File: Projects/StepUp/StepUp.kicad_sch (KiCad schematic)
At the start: 0 parts

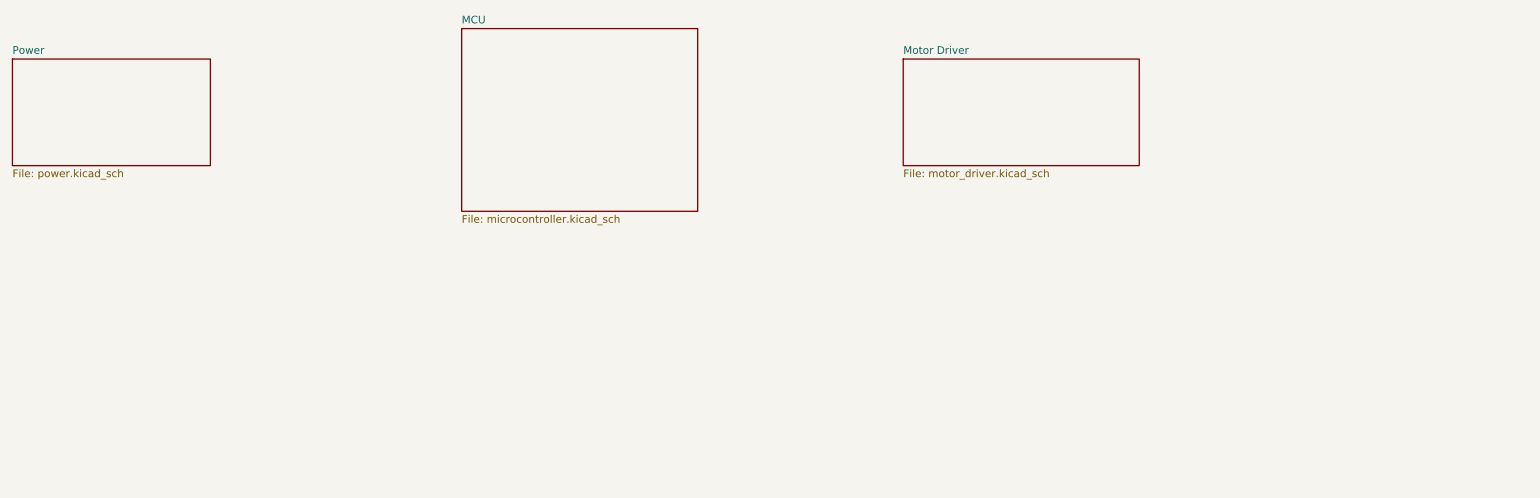
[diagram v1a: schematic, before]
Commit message: feat(rp2040): Layout begins, extra libraries
RPico minimal project downloaded + assets copied. Boost converter layout
in progress, 18650 battery holder added.
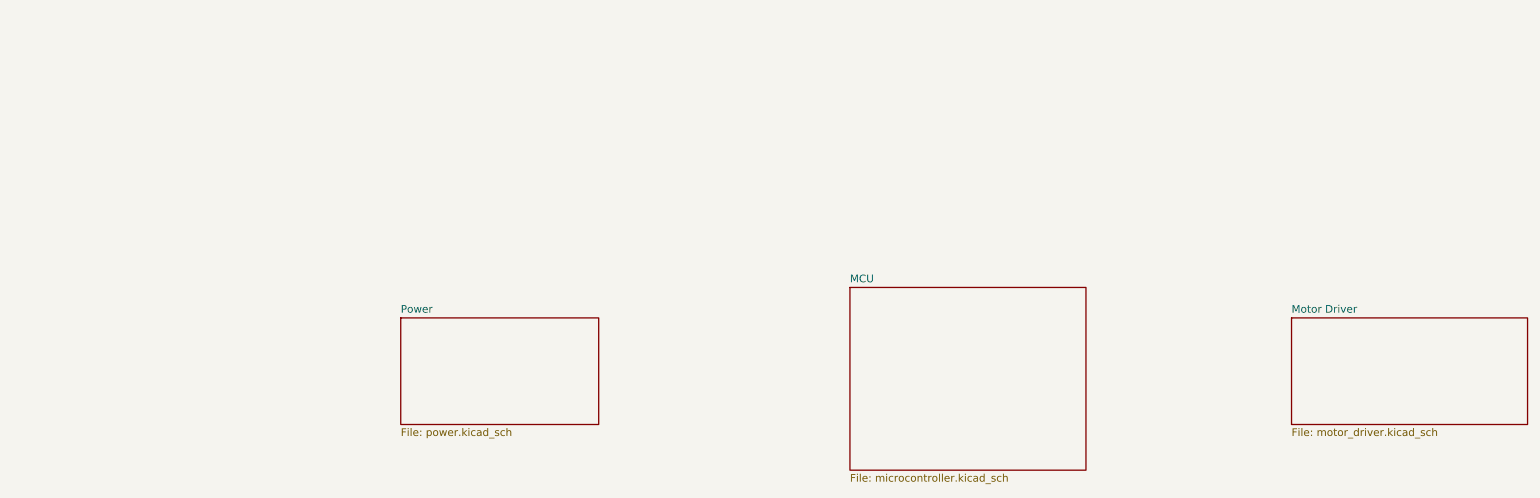
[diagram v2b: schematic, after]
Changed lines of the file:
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@@
 	(generator "eeschema")
 	(generator_version "8.0")
-	(paper "A4")
+	(paper "A3")
 	(title_block
 		(title "System diagram")
@@
 	)
 	(sheet
-		(at 125.73 80.01)
+		(at 190.5 123.19)
 		(size 39.37 30.48)
 		(fields_autoplaced yes)
@@
 		)
 		(property "Sheetname" "MCU"
-			(at 125.73 79.2984 0)
+			(at 190.5 122.4784 0)
 			(effects
 				(font
@@
 		)
 		(property "Sheetfile" "microcontroller.kicad_sch"
-			(at 125.73 111.0746 0)
+			(at 190.5 154.2546 0)
 			(effects
 				(font
@@
 	)
 	(sheet
-		(at 50.8 85.09)
+		(at 115.57 128.27)
 		(size 33.02 17.78)
 		(fields_autoplaced yes)
@@
 		)
 		(property "Sheetname" "Power"
-			(at 50.8 84.3784 0)
+			(at 115.57 127.5584 0)
 			(effects
 				(font
@@
 		)
 		(property "Sheetfile" "power.kicad_sch"
-			(at 50.8 103.4546 0)
+			(at 115.57 146.6346 0)
 			(effects
 				(font
@@
 	)
 	(sheet
-		(at 199.39 85.09)
+		(at 264.16 128.27)
 		(size 39.37 17.78)
 		(fields_autoplaced yes)
@@
 		)
 		(property "Sheetname" "Motor Driver"
-			(at 199.39 84.3784 0)
+			(at 264.16 127.5584 0)
 			(effects
 				(font
@@
 		)
 		(property "Sheetfile" "motor_driver.kicad_sch"
-			(at 199.39 103.4546 0)
+			(at 264.16 146.6346 0)
 			(effects
 				(font

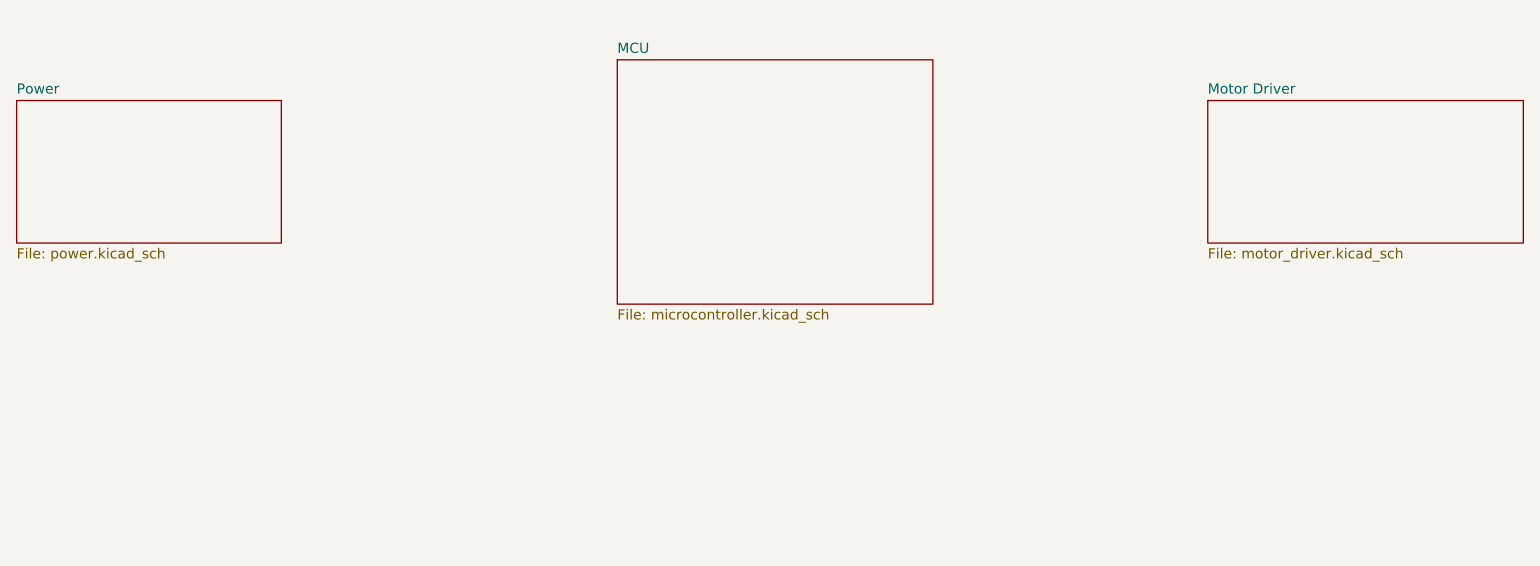
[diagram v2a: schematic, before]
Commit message: feat(joystick): Added part
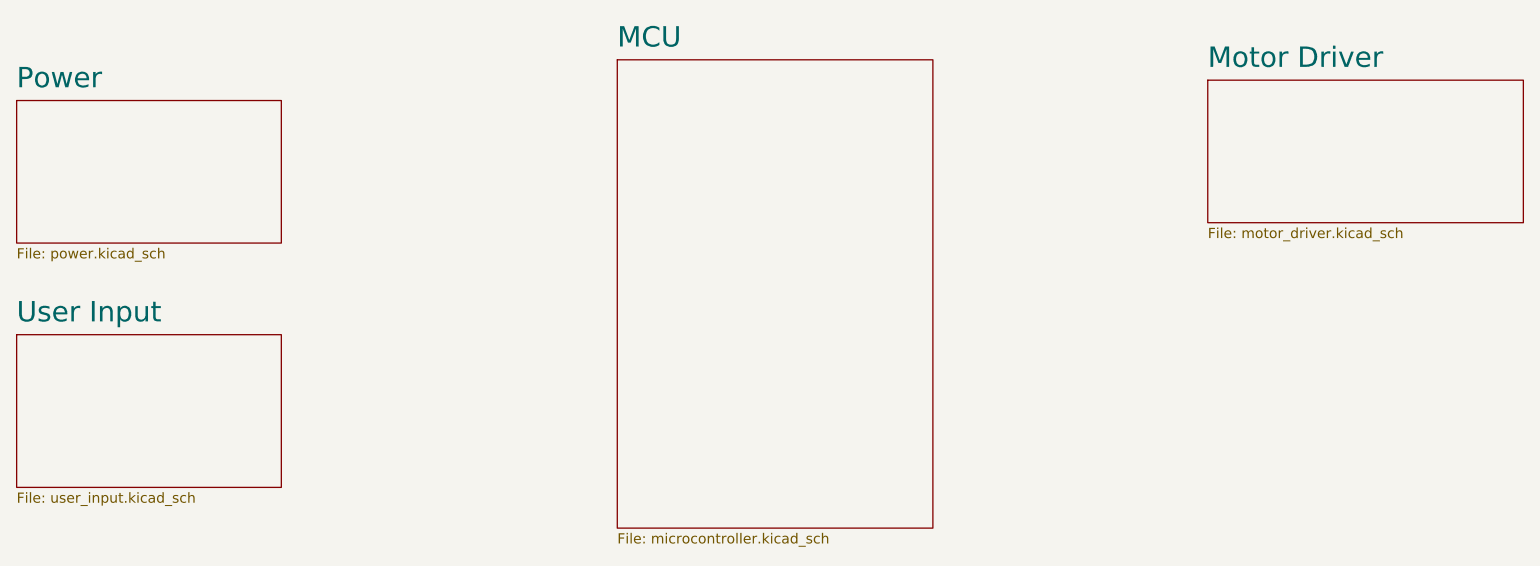
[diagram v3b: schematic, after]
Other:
- added sheet User Input (user_input.kicad_sch)
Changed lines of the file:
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@@
 	(sheet
 		(at 190.5 123.19)
-		(size 39.37 30.48)
+		(size 39.37 58.42)
 		(fields_autoplaced yes)
 		(stroke
@@
 		)
 		(property "Sheetname" "MCU"
-			(at 190.5 122.4784 0)
+			(at 190.5 121.8434 0)
 			(effects
 				(font
-					(size 1.27 1.27)
+					(size 2.54 2.54)
 				)
 				(justify left bottom)
@@
 		)
 		(property "Sheetfile" "microcontroller.kicad_sch"
-			(at 190.5 154.2546 0)
+			(at 190.5 182.1946 0)
 			(effects
 				(font
@@
 	)
 	(sheet
+		(at 115.57 157.48)
+		(size 33.02 19.05)
+		(fields_autoplaced yes)
+		(stroke
+			(width 0.1524)
+			(type solid)
+		)
+		(fill
+			(color 255 255 194 1.0000)
+		)
+		(property "Sheetname" "User Input"
+			(at 115.57 156.1334 0)
+			(effects
+				(font
+					(size 2.54 2.54)
+				)
+				(justify left bottom)
+			)
+		)
+		(property "Sheetfile" "user_input.kicad_sch"
+			(at 115.57 177.1146 0)
+			(effects
+				(font
+					(size 1.27 1.27)
+				)
+				(justify left top)
+			)
+		)
+		(instances
+			(project "StepUp"
+				(path "/e0cca1c7-c263-49eb-8c40-74000ebe5285"
+					(page "6")
+				)
+			)
+		)
+	)
+	(sheet
 		(at 115.57 128.27)
 		(size 33.02 17.78)
@@
 		)
 		(property "Sheetname" "Power"
-			(at 115.57 127.5584 0)
+			(at 115.57 126.9234 0)
 			(effects
 				(font
-					(size 1.27 1.27)
+					(size 2.54 2.54)
 				)
 				(justify left bottom)
@@
 	)
 	(sheet
-		(at 264.16 128.27)
+		(at 264.16 125.73)
 		(size 39.37 17.78)
 		(fields_autoplaced yes)
@@
 		)
 		(property "Sheetname" "Motor Driver"
-			(at 264.16 127.5584 0)
+			(at 264.16 124.3834 0)
 			(effects
 				(font
-					(size 1.27 1.27)
+					(size 2.54 2.54)
 				)
 				(justify left bottom)
@@
 		)
 		(property "Sheetfile" "motor_driver.kicad_sch"
-			(at 264.16 146.6346 0)
+			(at 264.16 144.0946 0)
 			(effects
 				(font

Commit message: feat(stepup): Many additions
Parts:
- added H1, H2, H3, H4: MountingHole, MountingHole:MountingHole_2.7mm_M2.5, symbol Mechanical:MountingHole
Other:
- added sheet LEDs (leds.kicad_sch)

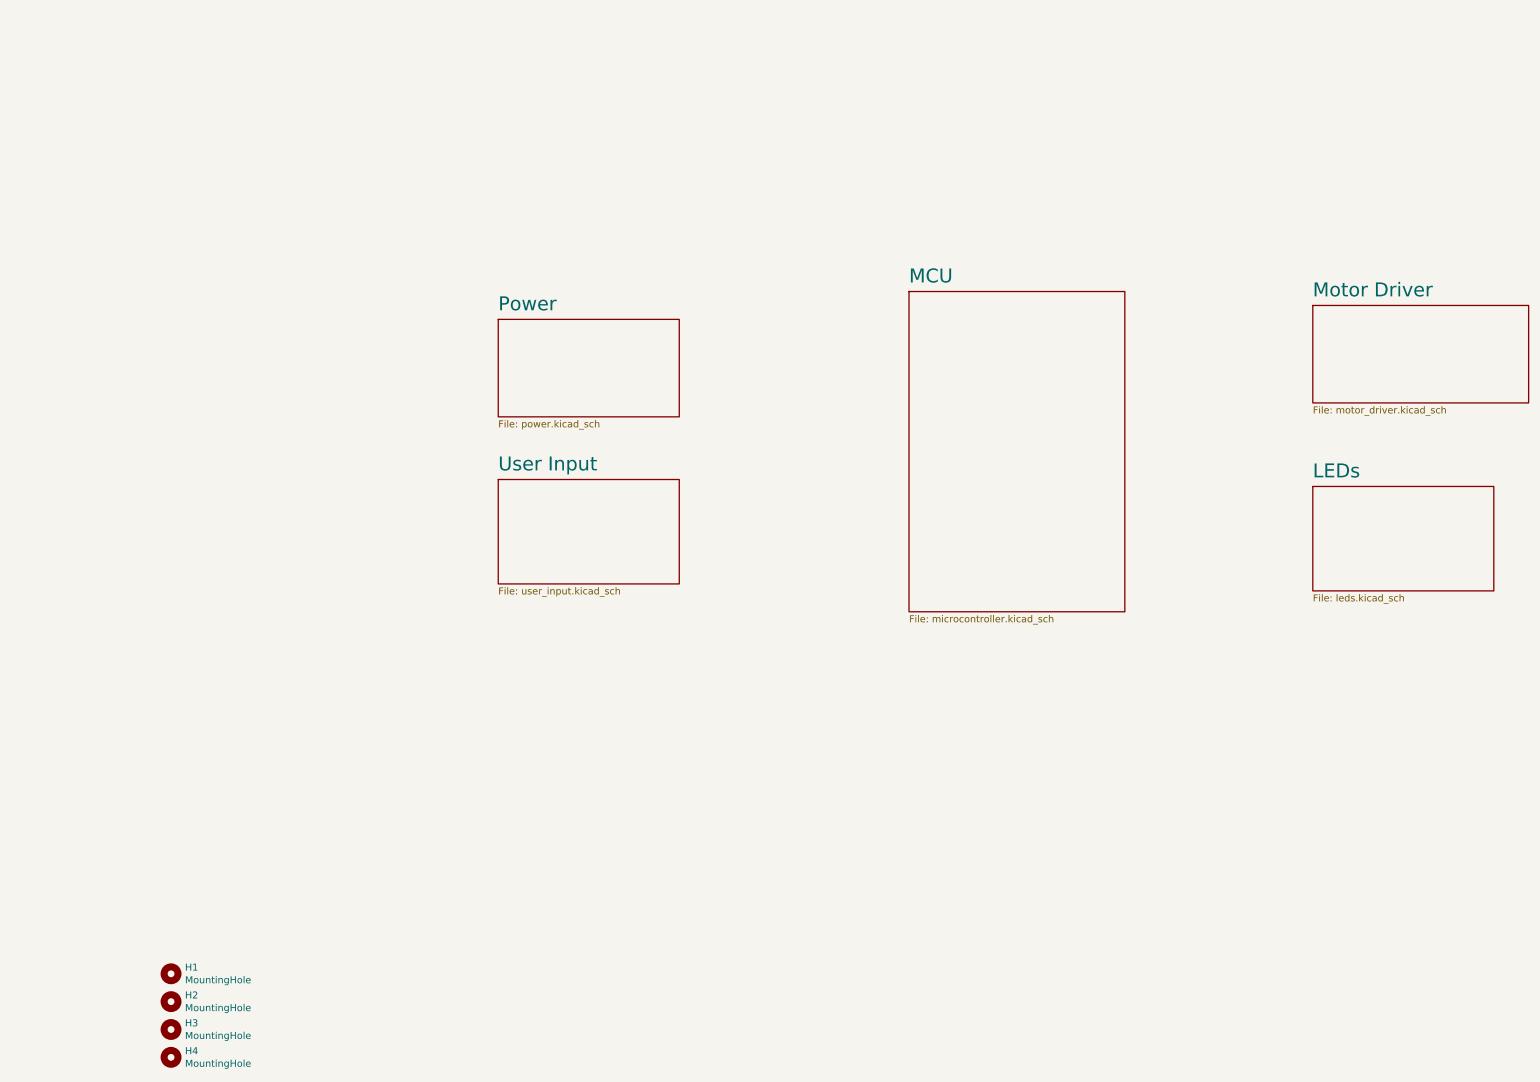
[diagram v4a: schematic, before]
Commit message: feat(schematic): Ready for layout
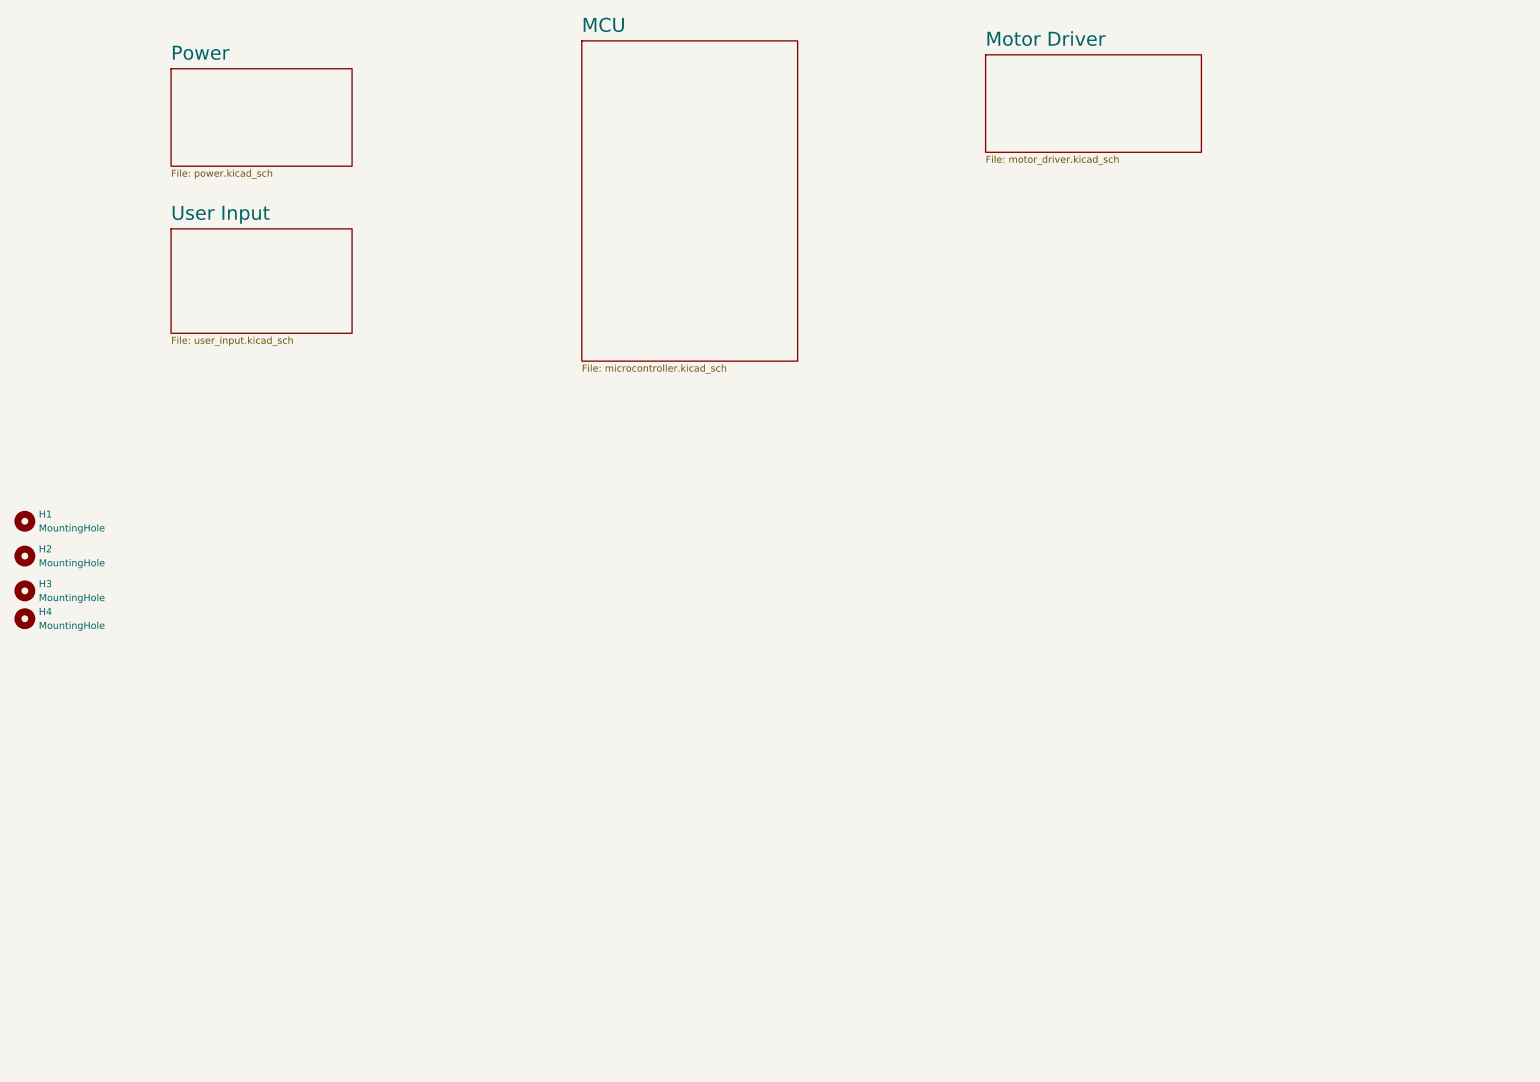
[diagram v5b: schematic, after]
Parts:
- H1, H2, H3, H4: footprint MountingHole:MountingHole_2.7mm_M2.5 -> MountingHole:MountingHole_3.2mm_M3
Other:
- removed sheet LEDs

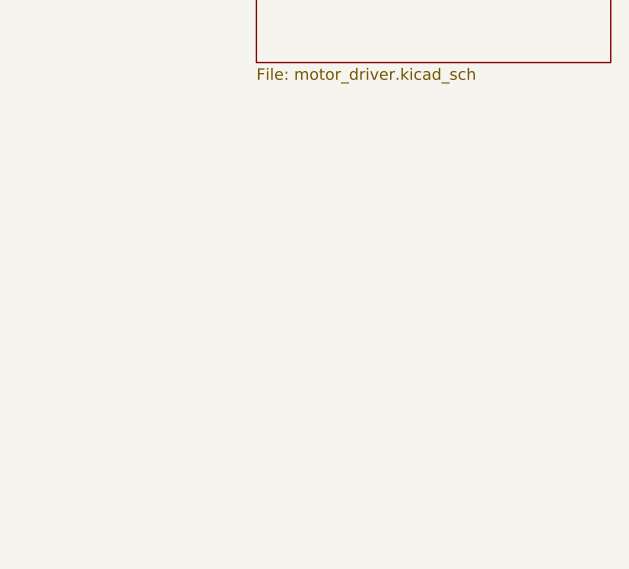
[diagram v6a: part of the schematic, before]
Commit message: feat(tidy): Bigger PMOS, added footprints
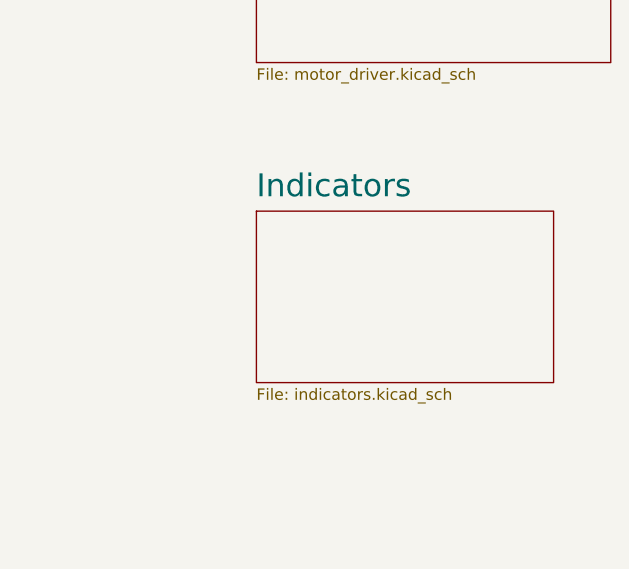
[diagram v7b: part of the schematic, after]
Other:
- added sheet Indicators (indicators.kicad_sch)
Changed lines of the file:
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@@
+	)
+	(sheet
+		(at 204.47 114.3)
+		(size 33.02 19.05)
+		(fields_autoplaced yes)
+		(stroke
+			(width 0.1524)
+			(type solid)
+		)
+		(fill
+			(color 255 255 194 1.0000)
+		)
+		(property "Sheetname" "Indicators"
+			(at 204.47 112.9534 0)
+			(effects
+				(font
+					(size 2.54 2.54)
+				)
+				(justify left bottom)
+			)
+		)
+		(property "Sheetfile" "indicators.kicad_sch"
+			(at 204.47 133.9346 0)
+			(effects
+				(font
+					(size 1.27 1.27)
+				)
+				(justify left top)
+			)
+		)
+		(instances
+			(project "StepUp"
+				(path "/e0cca1c7-c263-49eb-8c40-74000ebe5285"
+					(page "5")
+				)
+			)
+		)
 	)
 	(sheet
